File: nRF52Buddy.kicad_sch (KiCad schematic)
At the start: 4 parts

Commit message: Updates for revision 2
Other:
- sheet Connectors ports: added P1.09/~{CHARGE}; removed P1.09
- sheet Power Input ports: added P1.09/~{CHARGE}; removed none

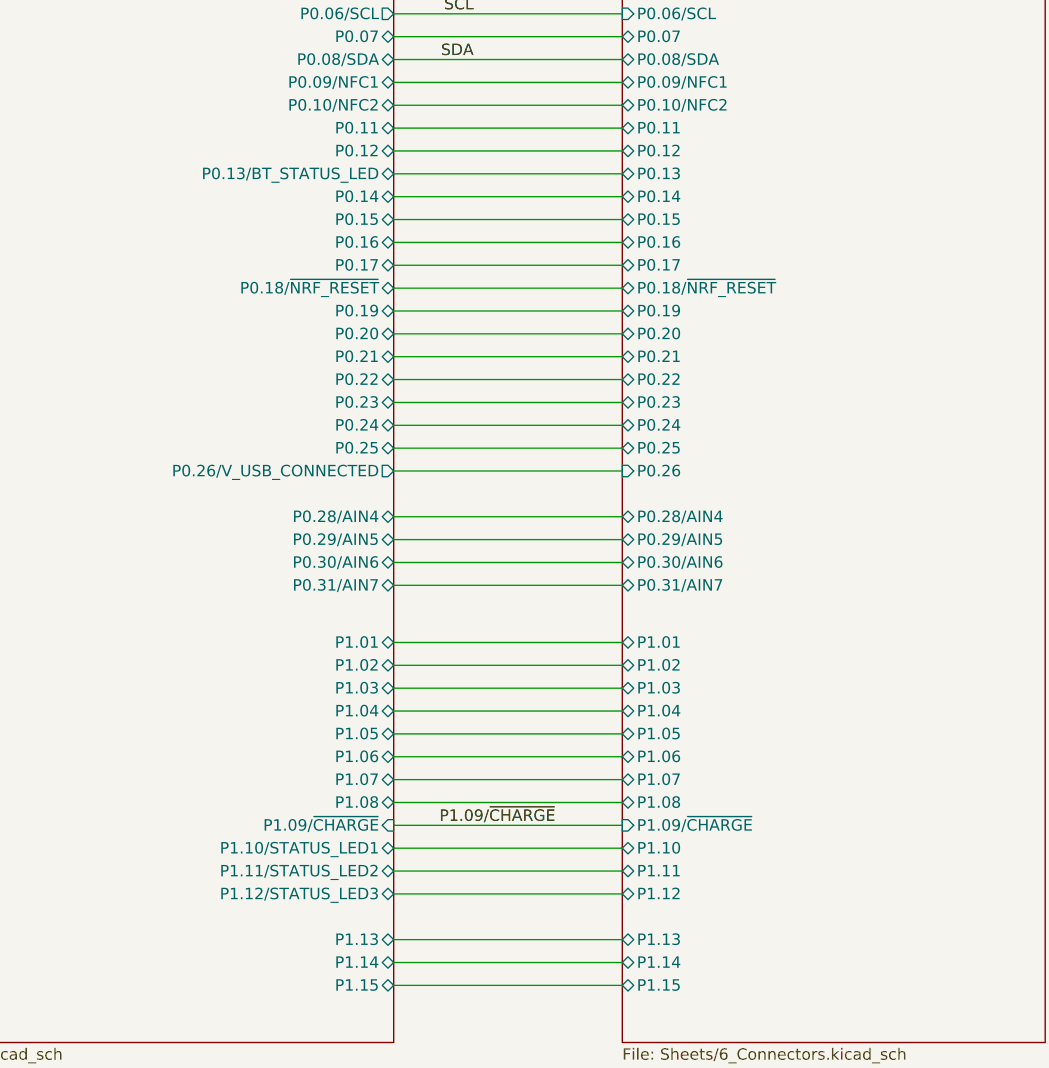
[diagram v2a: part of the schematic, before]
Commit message: changed LED net names to indicate status LEDs and changed 3V3 pin on mezzanine connector to be GND
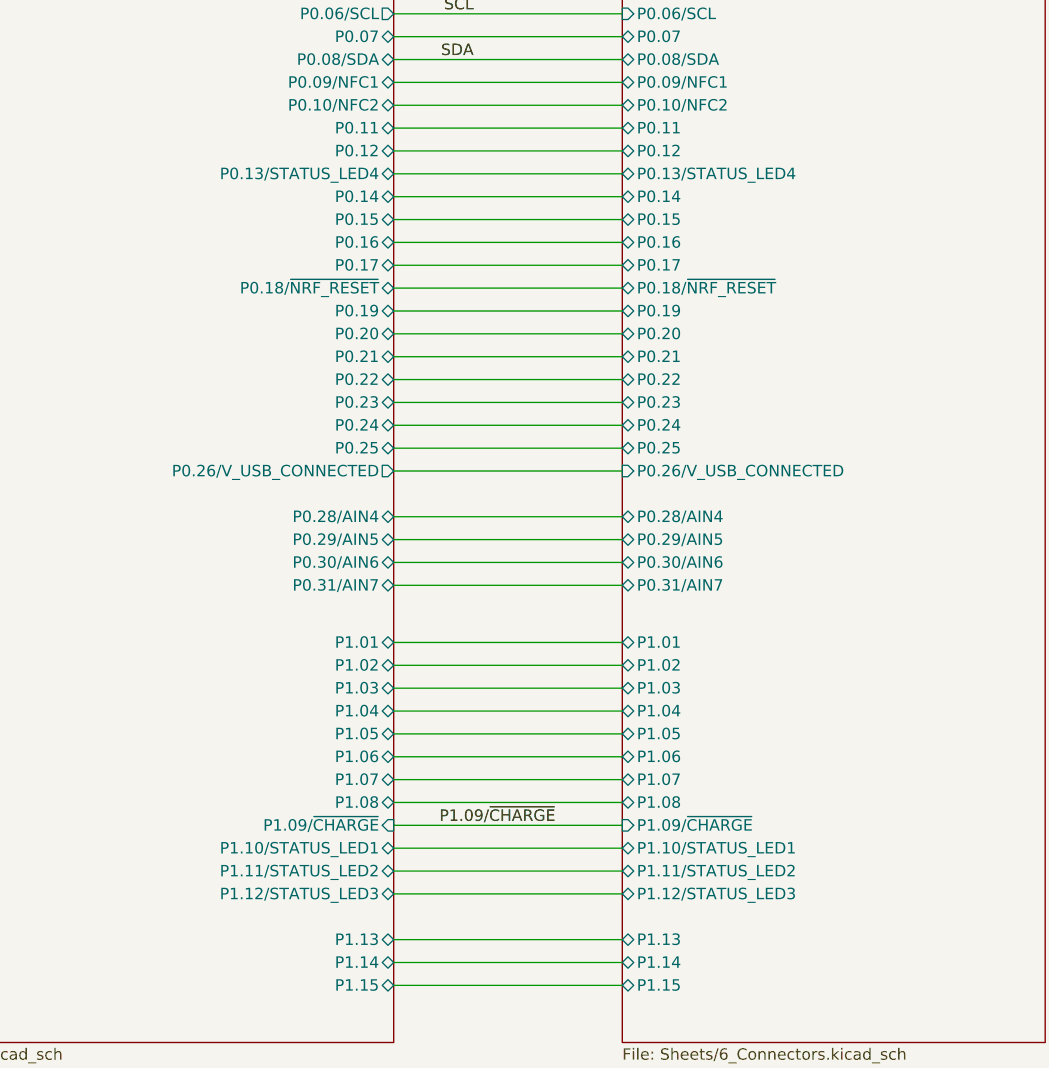
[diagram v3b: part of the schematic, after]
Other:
- sheet Connectors ports: added P0.13/STATUS_LED4, P0.26/V_USB_CONNECTED, P1.10/STATUS_LED1, P1.11/STATUS_LED2, P1.12/STATUS_LED3; removed P0.13, P0.26, P1.10, P1.11, P1.12
- sheet MCU (nRF52840) ports: added P0.13/STATUS_LED4; removed P0.13/BT_STATUS_LED
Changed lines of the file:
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@@
       (effects (font (size 1.27 1.27)) (justify left top))
     )
-    (pin "P1.10" bidirectional (at 217.17 125.73 180)
-      (effects (font (size 1.27 1.27)) (justify left))
-    )
-    (pin "P1.12" bidirectional (at 217.17 130.81 180)
-      (effects (font (size 1.27 1.27)) (justify left))
-    )
-    (pin "P1.11" bidirectional (at 217.17 128.27 180)
-      (effects (font (size 1.27 1.27)) (justify left))
-    )
-    (pin "P0.26" input (at 217.17 83.82 180)
-      (effects (font (size 1.27 1.27)) (justify left))
-    )
-    (pin "P0.13" bidirectional (at 217.17 50.8 180)
+    (pin "P1.10{slash}STATUS_LED1" bidirectional (at 217.17 125.73 180)
+      (effects (font (size 1.27 1.27)) (justify left))
+    )
+    (pin "P1.12{slash}STATUS_LED3" bidirectional (at 217.17 130.81 180)
+      (effects (font (size 1.27 1.27)) (justify left))
+    )
+    (pin "P1.11{slash}STATUS_LED2" bidirectional (at 217.17 128.27 180)
+      (effects (font (size 1.27 1.27)) (justify left))
+    )
+    (pin "P0.26{slash}V_USB_CONNECTED" input (at 217.17 83.82 180)
+      (effects (font (size 1.27 1.27)) (justify left))
+    )
+    (pin "P0.13{slash}STATUS_LED4" bidirectional (at 217.17 50.8 180)
       (effects (font (size 1.27 1.27)) (justify left))
     )
@@
       (effects (font (size 1.27 1.27)) (justify left))
     )
-    (pin "P0.13{slash}BT_STATUS_LED" bidirectional (at 191.77 50.8 0)
-      (effects (font (size 1.27 1.27)) (justify right))
-    )
+    (pin "P0.13{slash}STATUS_LED4" bidirectional (at 191.77 50.8 0)
+      (effects (font (size 1.27 1.27)) (justify right))
+    )
